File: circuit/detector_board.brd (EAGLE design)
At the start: 60 x 60 mm, 10 parts

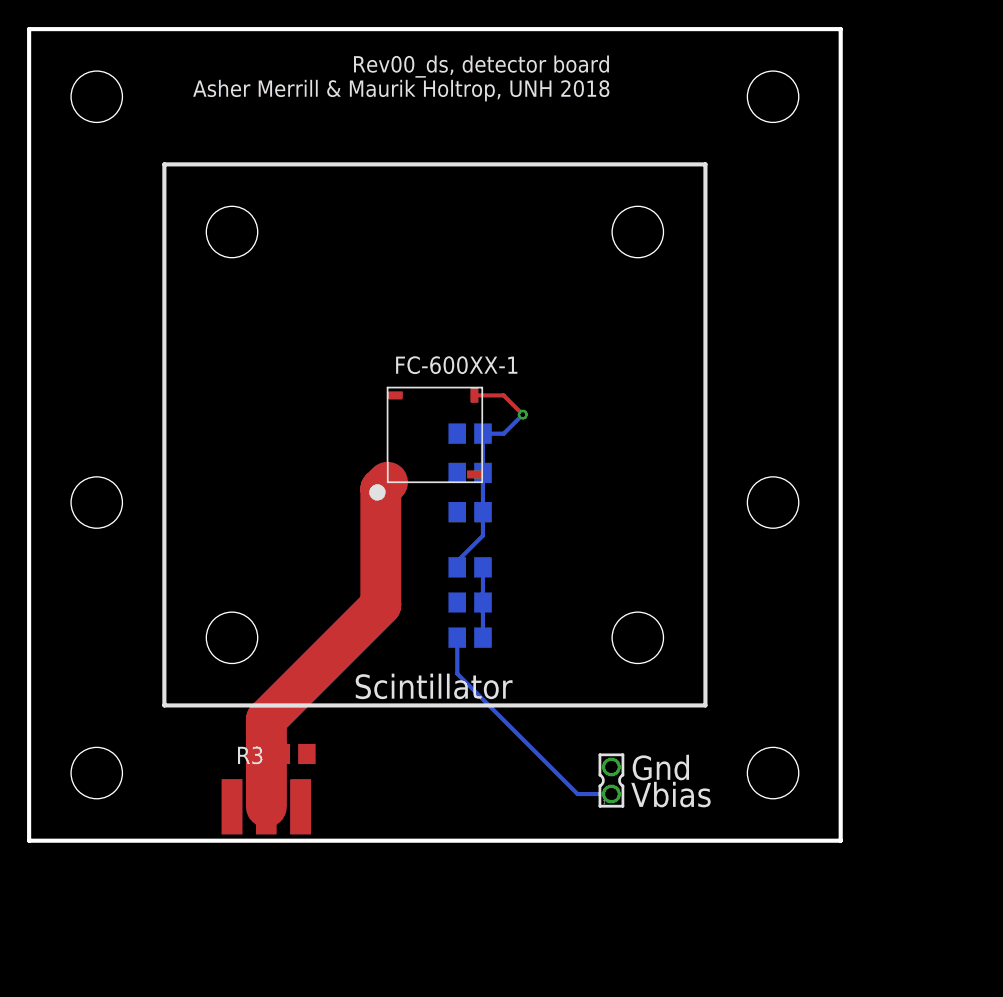
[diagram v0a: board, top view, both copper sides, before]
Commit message: Modified board. Tried to add Spice model.
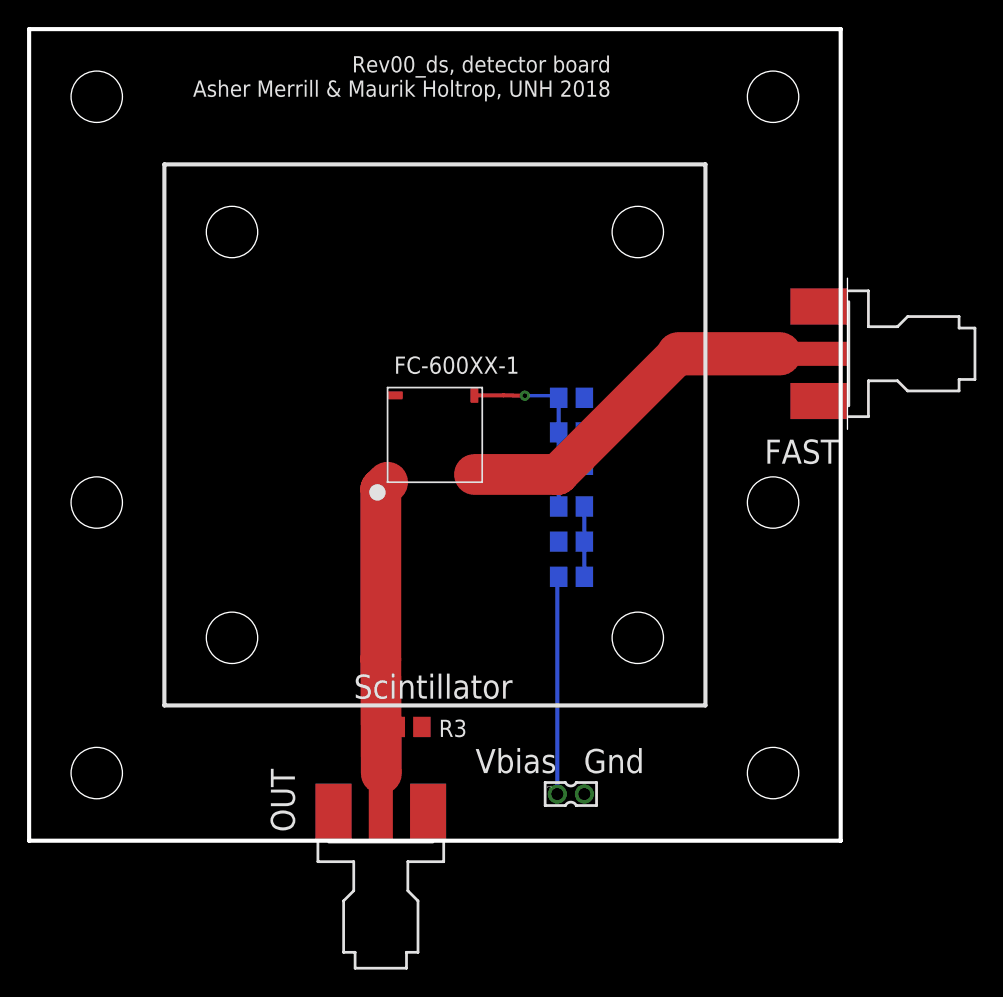
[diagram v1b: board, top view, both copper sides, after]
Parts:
- removed J$1: SMA_EDGE, SparkFun-Retired:SMA-EDGE
- added FAST, OUT: SMA-EDGE, 000phys605parts:SMA-EDGE
- FC-600XX-1: device 000phys605parts:FC-600XX-SMT_BLANK5 -> 000phys605parts:FC-600XX-SMT
- moved R1 8.75 mm to (40.1, 19.5)
- moved C1 8.75 mm to (40.1, 22.1)
- moved R2 8.75 mm to (40.1, 24.7)
- moved R3 8.73 mm to (28.1, 8.41)
- moved C2 8.28 mm to (40.1, 27.8), turned to 180 degrees
- moved C3 8.08 mm to (40.1, 30.2), turned to 180 degrees
- moved C4 7.95 mm to (40.1, 32.7), turned to 180 degrees
- moved SRC 3.16 mm to (40.0, 3.45), turned to 270 degrees
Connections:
- new net N$2: FAST.G@0, FC-600XX-1.F_FAST
- net GND: now also FAST.G@1, FAST.G@2, FAST.G@3, FAST.G@4, OUT.G@1, OUT.G@2, OUT.G@3, OUT.G@4; no longer J$1.GND@0, J$1.GND@1, J$1.GND@2, J$1.GND@3
- net V_AN: now also OUT.G@0; no longer J$1.SIG
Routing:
- net N$2: track 0.00 -> 26.3 mm
- net V_AN: track 29.9 -> 22.6 mm
- net VBIAS: track 18.4 -> 14.3 mm
- net N$4: track 17.7 -> 16.1 mm
